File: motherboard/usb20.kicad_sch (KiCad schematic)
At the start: 11 parts, among them J16 USB, J17 USB, J18 USB, J19 USB, U22 CH334F, Y2 12MHz

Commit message: major power work
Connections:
- no-connect marks 17 -> 19
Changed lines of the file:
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@@
 	(generator_version "8.99")
 	(paper "A4")
+	(text "spare"
+		(exclude_from_sim no)
+		(at 102.616 137.668 0)
+		(effects
+			(font
+				(size 1.27 1.27)
+			)
+		)
+	)
 	(text "trackpad"
 		(exclude_from_sim no)
@@
 	)
 	(no_connect
+		(at 97.79 135.89)
+	)
+	(no_connect
 		(at 158.1059 111.0285)
 	)
@@
 		(at 100.33 81.28)
 	)
+	(no_connect
+		(at 97.79 138.43)
+	)
 	(wire

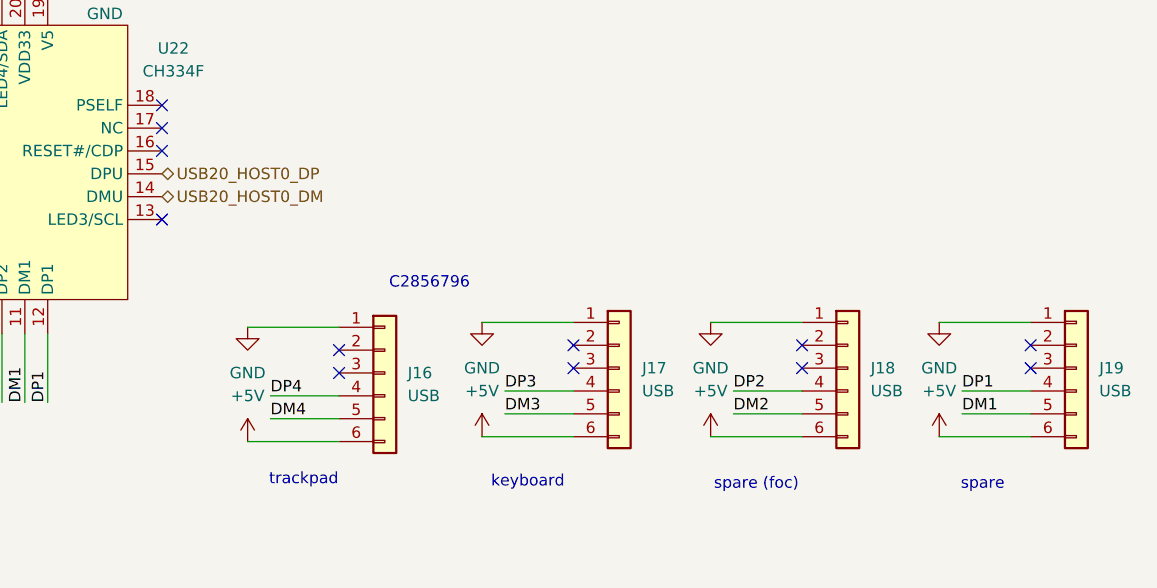
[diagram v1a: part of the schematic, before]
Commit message: synchronizing hierarchical pins
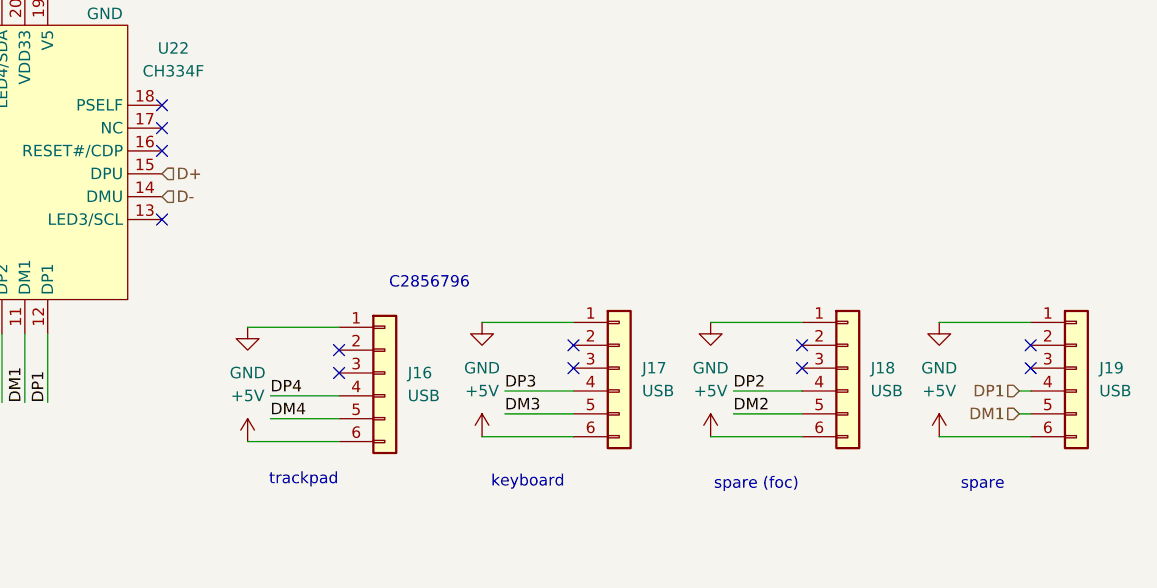
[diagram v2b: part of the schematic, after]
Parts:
- C64, C65, C66, C67, C68: footprint (none) -> Capacitor_SMD:C_0402_1005Metric
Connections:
- net USB20_HOST0_DM renamed D-
- net USB20_HOST0_DP renamed D+
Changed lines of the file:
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@@
 	(wire
 		(pts
-			(xy 227.33 115.57) (xy 234.95 115.57)
+			(xy 233.68 115.57) (xy 234.95 115.57)
 		)
 		(stroke
@@
 	(wire
 		(pts
-			(xy 227.33 113.03) (xy 234.95 113.03)
+			(xy 233.68 113.03) (xy 234.95 113.03)
 		)
 		(stroke
@@
 		)
 	)
-	(label "DM1"
-		(at 227.33 115.57 0)
-		(fields_autoplaced yes)
-		(effects
-			(font
-				(size 1.27 1.27)
-			)
-			(justify left bottom)
-		)
-	)
 	(label "DP2"
 		(at 201.93 113.03 0)
@@
 		)
 	)
-	(label "DP1"
-		(at 227.33 113.03 0)
-		(fields_autoplaced yes)
-		(effects
-			(font
-				(size 1.27 1.27)
-			)
-			(justify left bottom)
-		)
-	)
 	(label "X2"
 		(at 92.71 88.9 0)
@@
 		)
 	)
-	(hierarchical_label "USB20_HOST0_DM"
-		(shape bidirectional)
+	(hierarchical_label "D-"
+		(shape input)
 		(at 138.43 91.44 0)
 		(fields_autoplaced yes)
@@
 		)
 	)
-	(hierarchical_label "USB20_HOST0_DP"
-		(shape bidirectional)
+	(hierarchical_label "DM1"
+		(shape input)
+		(at 233.68 115.57 180)
+		(fields_autoplaced yes)
+		(effects
+			(font
+				(size 1.27 1.27)
+			)
+			(justify right)
+		)
+	)
+	(hierarchical_label "D+"
+		(shape input)
 		(at 138.43 88.9 0)
 		(fields_autoplaced yes)
@@
 		(shape bidirectional)
 		(at 97.79 138.43 180)
+		(fields_autoplaced yes)
+		(effects
+			(font
+				(size 1.27 1.27)
+			)
+			(justify right)
+		)
+	)
+	(hierarchical_label "DP1"
+		(shape input)
+		(at 233.68 113.03 180)
 		(fields_autoplaced yes)
 		(effects
@@
 			)
 		)
-		(property "Footprint" ""
+		(property "Footprint" "Capacitor_SMD:C_0402_1005Metric"
 			(at 132.08 63.5 0)
 			(effects
@@
 			)
 		)
-		(property "Footprint" ""
+		(property "Footprint" "Capacitor_SMD:C_0402_1005Metric"
 			(at 71.12 74.93 0)
 			(effects
@@
 			)
 		)
-		(property "Footprint" ""
+		(property "Footprint" "Capacitor_SMD:C_0402_1005Metric"
 			(at 113.03 63.5 0)
 			(effects
@@
 			)
 		)
-		(property "Footprint" ""
+		(property "Footprint" "Capacitor_SMD:C_0402_1005Metric"
 			(at 107.95 63.5 0)
 			(effects
@@
 			)
 		)
-		(property "Footprint" ""
+		(property "Footprint" "Capacitor_SMD:C_0402_1005Metric"
 			(at 82.55 74.93 0)
 			(effects

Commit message: linked all footprints
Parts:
- J16, J17, J18, J19: footprint (none) -> 6P_05mm_FPC:FPC-SMD_6P-P0.50_XUNPU_FPC-05F-6PH20
- Y2: footprint (none) -> Crystal:Crystal_SMD_2016-4Pin_2.0x1.6mm
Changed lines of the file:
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@@
 			)
 		)
-		(property "Footprint" ""
+		(property "Footprint" "6P_05mm_FPC:FPC-SMD_6P-P0.50_XUNPU_FPC-05F-6PH20"
 			(at 189.23 110.49 0)
 			(effects
@@
 			)
 		)
-		(property "Footprint" ""
+		(property "Footprint" "6P_05mm_FPC:FPC-SMD_6P-P0.50_XUNPU_FPC-05F-6PH20"
 			(at 240.03 110.49 0)
 			(effects
@@
 			)
 		)
-		(property "Footprint" ""
+		(property "Footprint" "6P_05mm_FPC:FPC-SMD_6P-P0.50_XUNPU_FPC-05F-6PH20"
 			(at 214.63 110.49 0)
 			(effects
@@
 			)
 		)
-		(property "Footprint" ""
+		(property "Footprint" "Crystal:Crystal_SMD_2016-4Pin_2.0x1.6mm"
 			(at 76.2 72.39 0)
 			(effects
@@
 			)
 		)
-		(property "Footprint" ""
+		(property "Footprint" "6P_05mm_FPC:FPC-SMD_6P-P0.50_XUNPU_FPC-05F-6PH20"
 			(at 163.1859 111.0285 0)
 			(effects

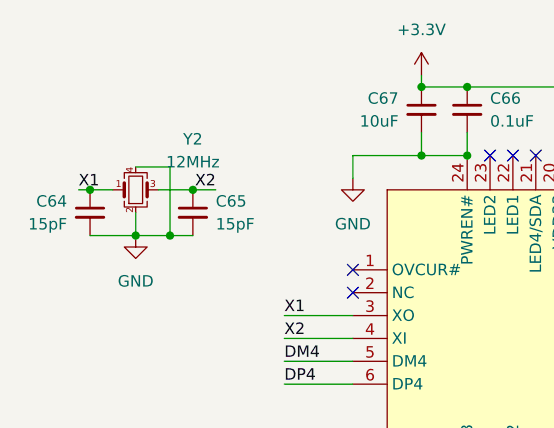
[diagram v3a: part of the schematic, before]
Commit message: cost optimizations for jlc
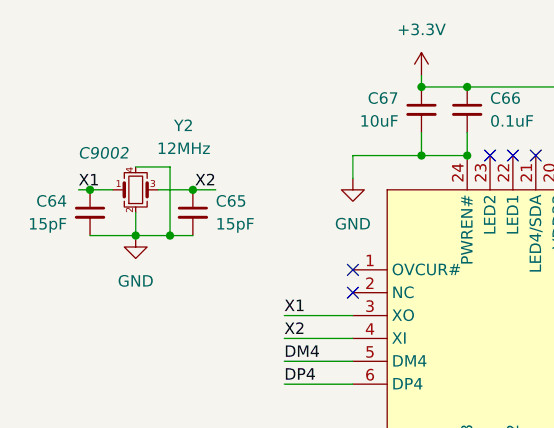
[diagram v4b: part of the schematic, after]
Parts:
- Y2: footprint Crystal:Crystal_SMD_2016-4Pin_2.0x1.6mm -> Crystal:Crystal_SMD_3225-4Pin_3.2x2.5mm
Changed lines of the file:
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@@
 			)
 		)
-		(property "Description" "Unpolarized capacitor, small symbol"
+		(property "Description" "C527590"
 			(at 107.95 63.5 0)
 			(effects
@@
 		(on_board yes)
 		(dnp no)
-		(fields_autoplaced yes)
 		(property "Reference" "Y2"
-			(at 82.55 66.7698 0)
+			(at 81.534 65.278 0)
 			(effects
 				(font
@@
 		)
 		(property "Value" "12MHz"
-			(at 82.55 69.3098 0)
+			(at 81.534 67.818 0)
 			(effects
 				(font
@@
 			)
 		)
-		(property "Footprint" "Crystal:Crystal_SMD_2016-4Pin_2.0x1.6mm"
+		(property "Footprint" "Crystal:Crystal_SMD_3225-4Pin_3.2x2.5mm"
 			(at 76.2 72.39 0)
 			(effects
@@
 			)
 		)
-		(property "Description" "Four pin crystal, GND on pins 2 and 4, small symbol"
-			(at 76.2 72.39 0)
+		(property "Description" "C9002"
+			(at 72.644 68.326 0)
 			(effects
 				(font
 					(size 1.27 1.27)
+					(italic yes)
 				)
-				(hide yes)
 			)
 		)

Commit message: work preparing for routing
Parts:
- J16, J17, J18, J19: symbol Connector_Generic:Conn_01x06 -> Connector_Generic_MountingPin:Conn_01x06_MountingPin
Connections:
- net GND: now also J16.MP (MountPin), J17.MP (MountPin), J18.MP (MountPin), J19.MP (MountPin), U22.25 (GND)

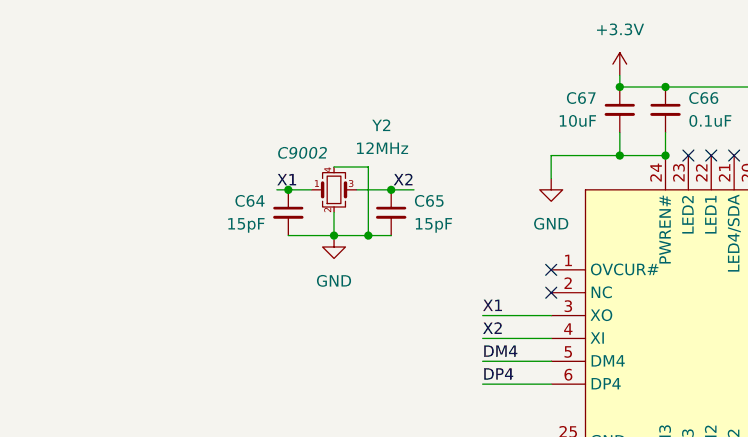
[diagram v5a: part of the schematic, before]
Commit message: component placement of I/O
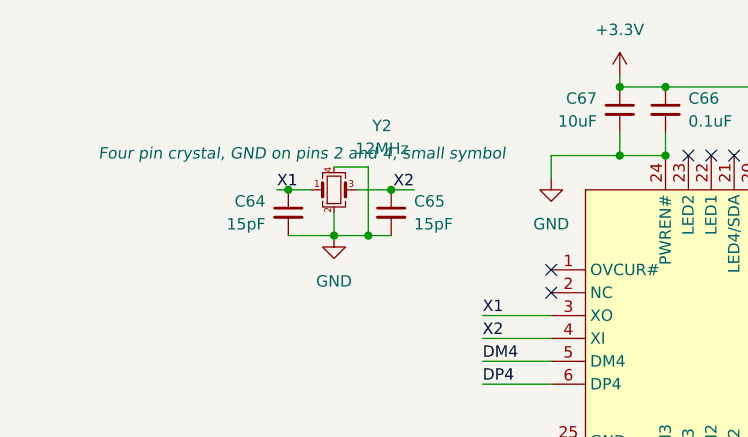
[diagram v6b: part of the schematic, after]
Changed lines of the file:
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@@
 			)
 		)
-		(property "Description" "Generic connector, single row, 01x06, script generated (kicad-library-utils/schlib/autogen/connector/)"
+		(property "Description" "Generic connectable mounting pin connector, single row, 01x06, script generated (kicad-library-utils/schlib/autogen/connector/)"
 			(at 189.23 110.49 0)
 			(effects
@@
 			)
 		)
-		(property "Description" "Generic connector, single row, 01x06, script generated (kicad-library-utils/schlib/autogen/connector/)"
+		(property "Description" "Generic connectable mounting pin connector, single row, 01x06, script generated (kicad-library-utils/schlib/autogen/connector/)"
 			(at 240.03 110.49 0)
 			(effects
@@
 			)
 		)
-		(property "Description" "Generic connector, single row, 01x06, script generated (kicad-library-utils/schlib/autogen/connector/)"
+		(property "Description" "Generic connectable mounting pin connector, single row, 01x06, script generated (kicad-library-utils/schlib/autogen/connector/)"
 			(at 214.63 110.49 0)
 			(effects
@@
 			)
 		)
-		(property "Description" "C527590"
+		(property "Description" "Unpolarized capacitor, small symbol"
 			(at 107.95 63.5 0)
 			(effects
@@
 			)
 		)
-		(property "Description" "C9002"
+		(property "Description" "Four pin crystal, GND on pins 2 and 4, small symbol"
 			(at 72.644 68.326 0)
 			(effects
@@
 			)
 		)
-		(property "Description" "Generic connector, single row, 01x06, script generated (kicad-library-utils/schlib/autogen/connector/)"
+		(property "Description" "Generic connectable mounting pin connector, single row, 01x06, script generated (kicad-library-utils/schlib/autogen/connector/)"
 			(at 162.56 110.49 0)
 			(effects

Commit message: layout nearing completion
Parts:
- added C17, C21, C4, C6: 10uF, Capacitor_SMD:C_0603_1608Metric, symbol Device:C_Small
- added C18, C22, C5, C7: 0.1uF, Capacitor_SMD:C_0402_1005Metric, symbol Device:C_Small
- C67: footprint Capacitor_SMD:C_0402_1005Metric -> Capacitor_SMD:C_0603_1608Metric
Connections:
- net +5V: now also C17.1, C18.1, C21.1, C22.1, C4.1, C5.1, C6.1, C7.1
- net GND: now also C17.2, C18.2, C21.2, C22.2, C4.2, C5.2, C6.2, C7.2

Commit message: v0.2 layout
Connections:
- no-connect marks 19 -> 17
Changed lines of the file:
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@@
 	(generator_version "8.99")
 	(paper "A4")
-	(text "spare"
-		(exclude_from_sim no)
-		(at 102.616 137.668 0)
-		(effects
-			(font
-				(size 1.27 1.27)
-			)
-		)
-	)
 	(text "trackpad"
 		(exclude_from_sim no)
@@
 	)
 	(no_connect
-		(at 97.79 135.89)
-	)
-	(no_connect
 		(at 157.48 110.49)
 	)
@@
 	(no_connect
 		(at 100.33 81.28)
-	)
-	(no_connect
-		(at 97.79 138.43)
 	)
 	(wire
@@
 		)
 	)
-	(hierarchical_label "USB20_HOST1_DM"
-		(shape bidirectional)
-		(at 97.79 138.43 180)
-		(fields_autoplaced yes)
-		(effects
-			(font
-				(size 1.27 1.27)
-			)
-			(justify right)
-		)
-	)
 	(hierarchical_label "DP1"
 		(shape input)
@@
 		(fields_autoplaced yes)
 		(effects
-			(font
-				(size 1.27 1.27)
-			)
-			(justify right)
-		)
-	)
-	(hierarchical_label "USB20_HOST1_DP"
-		(shape bidirectional)
-		(at 97.79 135.89 180)
-		(fields_autoplaced yes)
-		(effects
